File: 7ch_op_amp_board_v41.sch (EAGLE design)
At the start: 11 parts

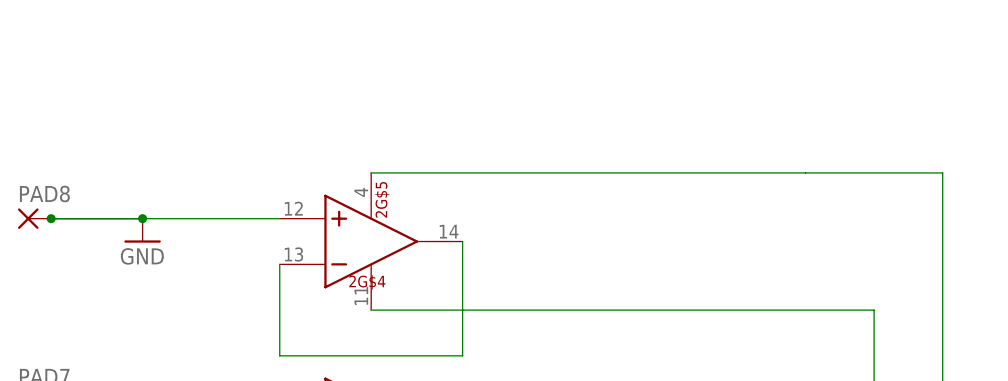
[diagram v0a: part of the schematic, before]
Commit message: Add through-hole for V+
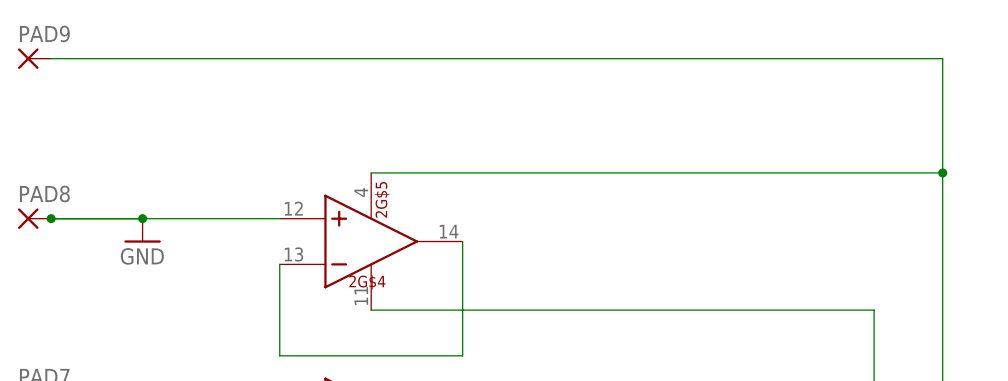
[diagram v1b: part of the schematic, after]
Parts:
- added PAD9: (no value), wirepad:1,6/0,9
- PAD1, PAD2, PAD3, PAD4, PAD5, PAD6, PAD7, PAD8: device wirepad:1,6/0,8 -> wirepad:1,6/0,9
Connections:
- net V+: now also PAD9.P
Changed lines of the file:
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@@
 <part name="1" library="kjbrown" deviceset="TL074-TSSOP" device="" value=""/>
 <part name="2" library="kjbrown" deviceset="TL074-TSSOP" device="" value=""/>
-<part name="PAD1" library="wirepad" deviceset="1,6/0,8" device=""/>
-<part name="PAD2" library="wirepad" deviceset="1,6/0,8" device=""/>
-<part name="PAD3" library="wirepad" deviceset="1,6/0,8" device=""/>
-<part name="PAD4" library="wirepad" deviceset="1,6/0,8" device=""/>
-<part name="PAD5" library="wirepad" deviceset="1,6/0,8" device=""/>
-<part name="PAD6" library="wirepad" deviceset="1,6/0,8" device=""/>
-<part name="PAD7" library="wirepad" deviceset="1,6/0,8" device=""/>
-<part name="PAD8" library="wirepad" deviceset="1,6/0,8" device=""/>
+<part name="PAD1" library="wirepad" deviceset="1,6/0,9" device=""/>
+<part name="PAD2" library="wirepad" deviceset="1,6/0,9" device=""/>
+<part name="PAD3" library="wirepad" deviceset="1,6/0,9" device=""/>
+<part name="PAD4" library="wirepad" deviceset="1,6/0,9" device=""/>
+<part name="PAD5" library="wirepad" deviceset="1,6/0,9" device=""/>
+<part name="PAD6" library="wirepad" deviceset="1,6/0,9" device=""/>
+<part name="PAD7" library="wirepad" deviceset="1,6/0,9" device=""/>
+<part name="PAD8" library="wirepad" deviceset="1,6/0,9" device=""/>
+<part name="PAD9" library="wirepad" deviceset="1,6/0,9" device=""/>
 </parts>
 <sheets>
@@
 <instance part="2" gate="G$4" x="-43.18" y="43.18"/>
 <instance part="2" gate="G$5" x="-43.18" y="43.18"/>
-<instance part="PAD1" gate="P" x="-78.74" y="-81.28"/>
-<instance part="PAD2" gate="P" x="-78.74" y="-66.04"/>
-<instance part="PAD3" gate="P" x="-78.74" y="-50.8"/>
-<instance part="PAD4" gate="P" x="-78.74" y="-30.48"/>
-<instance part="PAD5" gate="P" x="-81.28" y="-7.62"/>
-<instance part="PAD6" gate="P" x="-81.28" y="7.62"/>
-<instance part="PAD7" gate="P" x="-81.28" y="25.4"/>
-<instance part="PAD8" gate="P" x="-81.28" y="45.72"/>
+<instance part="PAD1" gate="1" x="-78.74" y="-81.28"/>
+<instance part="PAD2" gate="1" x="-78.74" y="-66.04"/>
+<instance part="PAD3" gate="1" x="-78.74" y="-50.8"/>
+<instance part="PAD4" gate="1" x="-78.74" y="-30.48"/>
+<instance part="PAD5" gate="1" x="-81.28" y="-7.62"/>
+<instance part="PAD6" gate="1" x="-81.28" y="7.62"/>
+<instance part="PAD7" gate="1" x="-81.28" y="25.4"/>
+<instance part="PAD8" gate="1" x="-81.28" y="45.72"/>
+<instance part="PAD9" gate="1" x="-81.28" y="63.5"/>
 </instances>
 <busses>
@@
 <junction x="20.32" y="-25.4"/>
 <pinref part="2" gate="G$5" pin="VCC+"/>
-<wire x1="20.32" y1="50.8" x2="5.08" y2="50.8" width="0.1524" layer="91"/>
-<wire x1="-43.18" y1="50.8" x2="5.08" y2="50.8" width="0.1524" layer="91"/>
+<wire x1="-43.18" y1="50.8" x2="20.32" y2="50.8" width="0.1524" layer="91"/>
+<pinref part="PAD9" gate="1" pin="P"/>
+<wire x1="-78.74" y1="63.5" x2="20.32" y2="63.5" width="0.1524" layer="91"/>
+<wire x1="20.32" y1="63.5" x2="20.32" y2="50.8" width="0.1524" layer="91"/>
+<junction x="20.32" y="50.8"/>
 </segment>
 </net>
@@
 <pinref part="2" gate="G$4" pin="IN+"/>
 <wire x1="-78.74" y1="45.72" x2="-68.58" y2="45.72" width="0.1524" layer="91"/>
-<pinref part="PAD8" gate="P" pin="P"/>
+<pinref part="PAD8" gate="1" pin="P"/>
 <junction x="-78.74" y="45.72"/>
 <wire x1="-68.58" y1="45.72" x2="-53.34" y2="45.72" width="0.1524" layer="91"/>
@@
 <segment>
 <pinref part="1" gate="G$1" pin="IN+"/>
-<pinref part="PAD1" gate="P" pin="P"/>
+<pinref part="PAD1" gate="1" pin="P"/>
 <wire x1="-76.2" y1="-81.28" x2="-55.88" y2="-81.28" width="0.1524" layer="91"/>
 </segment>
@@
 <segment>
 <pinref part="1" gate="G$2" pin="IN+"/>
-<pinref part="PAD2" gate="P" pin="P"/>
+<pinref part="PAD2" gate="1" pin="P"/>
 <wire x1="-76.2" y1="-66.04" x2="-55.88" y2="-66.04" width="0.1524" layer="91"/>
 </segment>
@@
 <segment>
 <pinref part="1" gate="G$3" pin="IN+"/>
-<pinref part="PAD3" gate="P" pin="P"/>
+<pinref part="PAD3" gate="1" pin="P"/>
 <wire x1="-76.2" y1="-50.8" x2="-55.88" y2="-50.8" width="0.1524" layer="91"/>
 </segment>
@@
 <segment>
 <pinref part="1" gate="G$4" pin="IN+"/>
-<pinref part="PAD4" gate="P" pin="P"/>
+<pinref part="PAD4" gate="1" pin="P"/>
 <wire x1="-76.2" y1="-30.48" x2="-55.88" y2="-30.48" width="0.1524" layer="91"/>
 </segment>
@@
 <segment>
 <pinref part="2" gate="G$3" pin="IN+"/>
-<pinref part="PAD7" gate="P" pin="P"/>
+<pinref part="PAD7" gate="1" pin="P"/>
 <wire x1="-53.34" y1="25.4" x2="-78.74" y2="25.4" width="0.1524" layer="91"/>
 </segment>
@@
 <segment>
 <pinref part="2" gate="G$2" pin="IN+"/>
-<pinref part="PAD6" gate="P" pin="P"/>
+<pinref part="PAD6" gate="1" pin="P"/>
 <wire x1="-53.34" y1="7.62" x2="-78.74" y2="7.62" width="0.1524" layer="91"/>
 </segment>
@@
 <segment>
 <pinref part="2" gate="G$1" pin="IN+"/>
-<pinref part="PAD5" gate="P" pin="P"/>
+<pinref part="PAD5" gate="1" pin="P"/>
 <wire x1="-53.34" y1="-7.62" x2="-78.74" y2="-7.62" width="0.1524" layer="91"/>
 </segment>
